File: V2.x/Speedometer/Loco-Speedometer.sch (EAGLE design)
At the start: 47 parts, among them IC1 Atmega 328-P, IC2 MCP2515, IC3 A1324LLHLT, Q1 8MHz, Q2 16MHz, U1 DRV8836, U2 ST732M50RSOT23-5L_STM, U3 DRV8836, U4 DRV8836

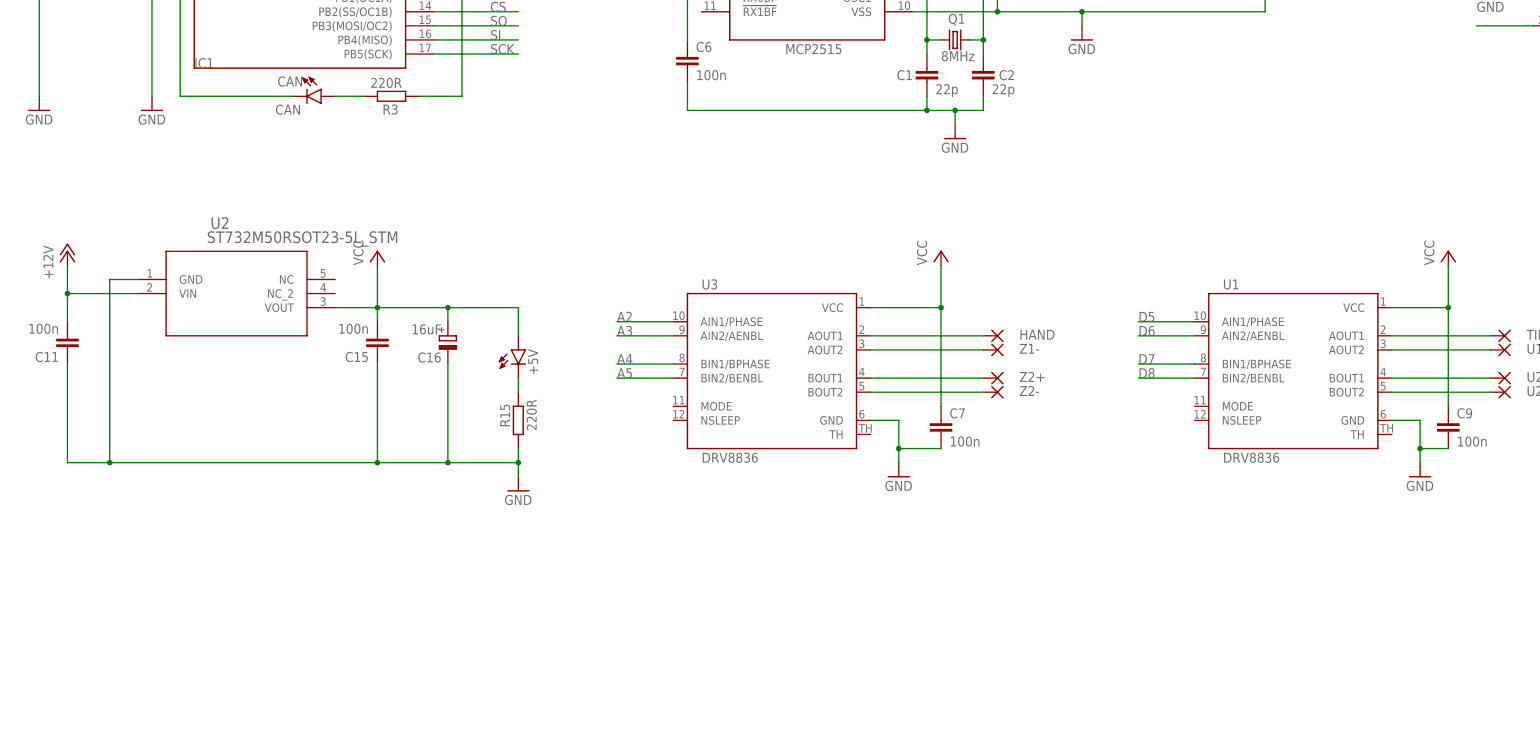
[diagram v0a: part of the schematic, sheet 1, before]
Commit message: Speedometer added mechanics with housing files added
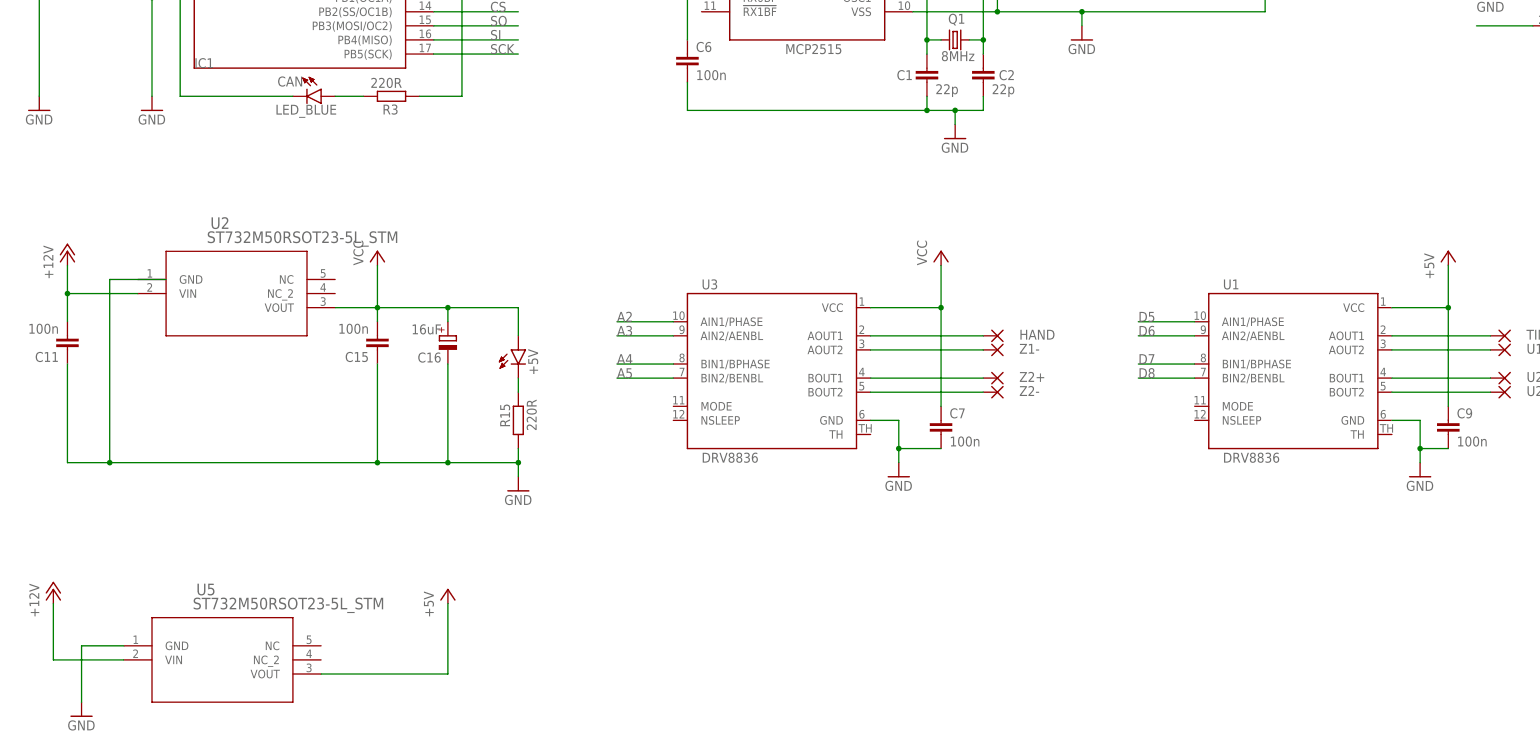
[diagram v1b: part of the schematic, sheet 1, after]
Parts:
- added U5: ST732M50RSOT23-5L_STM, ST732:ST732M50RSOT23-5L_STM
- +, +B, BELL, GND, H, HAND, L, TIME, U1-, U2+, U2-, Z1-, Z2+, Z2-: device wirepad:SMD2 -> wirepad:SMD1
- CAN: value CAN -> LED_BLUE
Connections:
- new net +5V: C9.1, U1.VCC, U5.VOUT
- net +12V: now also U5.VIN
- net GND: now also U5.GND
- net VCC: no longer C9.1, U1.VCC
